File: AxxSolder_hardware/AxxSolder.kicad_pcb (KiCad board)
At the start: 2 copper layers, 39 x 82.5 mm, 138 parts, among them IC1 TLV76733DRVR, IC2 OPA2387DSGT, IC3 LMR54406DBVR, IC4 STM32G431CBT6, IC5 TPD4E1U06DBVR, IC6 STUSB4500QTR, IC7 MAX16171ATA_VY+T, IC8 LTC4440AHMS8E, IC9 INA180A4IDBVT, J1 USB4110-GF-A, J2 691243110009, J3 TSW-102-07-T-S, J4 61300611821, J5 TSW-102-07-T-S, J6 TSW-102-07-T-S, Q1 STL9P3LLH6, Q2 STL10N3LLH5, Q3 2N7002NXAKR, U2 PEC11J-9215F-S0015, U3 BSC014N04LS

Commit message: Change IC9 from INA180 to INA281
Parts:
- IC9: value INA180A4IDBVT -> INA281A5QDBVRQ1
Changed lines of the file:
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@@
       (net 27 "/CC2") (pinfunction "1") (pintype "passive"))
   )
-  (footprint "footprints:SOT95P280X145-5N" (layer "B.Cu")
-    (at 188.95 107)
-    (descr "DBV (R-PDSO-G5)")
-    (tags "Integrated Circuit")
-    (property "Height" "1.45")
-    (property "Manufacturer_Name" "Texas Instruments")
-    (property "Manufacturer_Part_Number" "INA180A4IDBVT")
-    (property "Mouser Part Number" "595-INA180A4IDBVT")
-    (property "Mouser Price/Stock" "https://www.mouser.co.uk/ProductDetail/Texas-Instruments/INA180A4IDBVT?qs=5aG0NVq1C4zRWLlwoLPFOA%3D%3D")
-    (property "Sheetfile" "AxxSolder.kicad_sch")
-    (property "Sheetname" "")
-    (property "ki_description" "26V, 350kHz Bandwidth, Low- or High-Side Voltage Output Current Sense Amplifier")
-    (attr smd)
-    (fp_text reference "IC9" (at -0.55 2.35) (layer "B.SilkS")
-        (effects (font (size 0.8 0.8) (thickness 0.15) bold) (justify mirror))
-    )
-    (fp_text value "INA180A4IDBVT" (at 0 0) (layer "B.SilkS") hide
-        (effects (font (size 1.27 1.27) (thickness 0.254)) (justify mirror))
-    )
-    (fp_text user "${REFERENCE}" (at 0 0) (layer "B.Fab")
-        (effects (font (size 1.27 1.27) (thickness 0.254)) (justify mirror))
-    )
-    (fp_line (start -1.85 1.5) (end -0.65 1.5)
-      (stroke (width 0.2) (type solid)) (layer "B.SilkS"))
-    (fp_line (start -0.3 -1.45) (end -0.3 1.45)
-      (stroke (width 0.2) (type solid)) (layer "B.SilkS"))
-    (fp_line (start -0.3 1.45) (end 0.3 1.45)
-      (stroke (width 0.2) (type solid)) (layer "B.SilkS"))
-    (fp_line (start 0.3 -1.45) (end -0.3 -1.45)
-      (stroke (width 0.2) (type solid)) (layer "B.SilkS"))
-    (fp_line (start 0.3 1.45) (end 0.3 -1.45)
-      (stroke (width 0.2) (type solid)) (layer "B.SilkS"))
-    (fp_line (start -2.1 -1.775) (end -2.1 1.775)
-      (stroke (width 0.05) (type solid)) (layer "B.CrtYd"))
-    (fp_line (start -2.1 1.775) (end 2.1 1.775)
-      (stroke (width 0.05) (type solid)) (layer "B.CrtYd"))
-    (fp_line (start 2.1 -1.775) (end -2.1 -1.775)
-      (stroke (width 0.05) (type solid)) (layer "B.CrtYd"))
-    (fp_line (start 2.1 1.775) (end 2.1 -1.775)
-      (stroke (width 0.05) (type solid)) (layer "B.CrtYd"))
-    (fp_line (start -0.8 -1.45) (end -0.8 1.45)
-      (stroke (width 0.1) (type solid)) (layer "B.Fab"))
-    (fp_line (start -0.8 0.5) (end 0.15 1.45)
-      (stroke (width 0.1) (type solid)) (layer "B.Fab"))
-    (fp_line (start -0.8 1.45) (end 0.8 1.45)
-      (stroke (width 0.1) (type solid)) (layer "B.Fab"))
-    (fp_line (start 0.8 -1.45) (end -0.8 -1.45)
-      (stroke (width 0.1) (type solid)) (layer "B.Fab"))
-    (fp_line (start 0.8 1.45) (end 0.8 -1.45)
-      (stroke (width 0.1) (type solid)) (layer "B.Fab"))
-    (pad "1" smd rect (at -1.25 0.95 270) (size 0.6 1.2) (layers "B.Cu" "B.Paste" "B.Mask")
-      (net 81 "/I_LEAK") (pinfunction "OUT") (pintype "output"))
-    (pad "2" smd rect (at -1.25 0 270) (size 0.6 1.2) (layers "B.Cu" "B.Paste" "B.Mask")
-      (net 15 "GND") (pinfunction "GND") (pintype "power_in"))
-    (pad "3" smd rect (at -1.25 -0.95 270) (size 0.6 1.2) (layers "B.Cu" "B.Paste" "B.Mask")
-      (net 82 "Net-(IC9-IN+)") (pinfunction "IN+") (pintype "input"))
-    (pad "4" smd rect (at 1.25 -0.95 270) (size 0.6 1.2) (layers "B.Cu" "B.Paste" "B.Mask")
-      (net 63 "Earth") (pinfunction "IN-") (pintype "input"))
-    (pad "5" smd rect (at 1.25 0.95 270) (size 0.6 1.2) (layers "B.Cu" "B.Paste" "B.Mask")
-      (net 2 "+3.3V") (pinfunction "VS") (pintype "power_in"))
-    (model "${KIPRJMOD}/3rd-parties-libraries/3D-models/INA180A4IDBVT.stp"
-      (offset (xyz 0 0 0))
-      (scale (xyz 1 1 1))
-      (rotate (xyz 0 0 0))
-    )
-  )
   (footprint "Resistor_SMD:R_0805_2012Metric" (layer "B.Cu")
     (at 189.6 103.1125 90)
@@
       (offset (xyz 0 0 0))
       (scale (xyz 1 1 1))
+      (rotate (xyz 0 0 0))
+    )
+  )
+  (footprint "footprints:SOT95P280X145-5N" (layer "B.Cu")
+    (at 188.95 107)
+    (descr "DBV (R-PDSO-G5)")
+    (tags "Integrated Circuit")
+    (property "Height" "1.45")
+    (property "Manufacturer_Name" "Texas Instruments")
+    (property "Manufacturer_Part_Number" "INA281A5QDBVRQ1")
+    (property "Mouser Part Number" "595-INA281A5QDBVRQ1")
+    (property "Mouser Price/Stock" "https://www.mouser.co.uk/ProductDetail/Texas-Instruments/INA281A5QDBVRQ1?qs=hd1VzrDQEGgwv71iGabWgQ%3D%3D")
+    (property "Sheetfile" "AxxSolder.kicad_sch")
+    (property "Sheetname" "")
+    (property "ki_description" "Current Sense Amplifiers Automotive AEC-Q100, -4-V to 110-V, 1.3-MHz current sense amplifier 5-SOT-23 -40 to 125")
+    (attr smd)
+    (fp_text reference "IC9" (at -0.87 2.29) (layer "B.SilkS")
+        (effects (font (size 0.8 0.8) (thickness 0.15) bold) (justify mirror))
+    )
+    (fp_text value "INA281A5QDBVRQ1" (at 0 0) (layer "B.SilkS") hide
+        (effects (font (size 1.27 1.27) (thickness 0.254)) (justify mirror))
+    )
+    (fp_text user "${REFERENCE}" (at 0 0) (layer "B.Fab")
+        (effects (font (size 1.27 1.27) (thickness 0.254)) (justify mirror))
+    )
+    (fp_line (start -1.85 1.5) (end -0.65 1.5)
+      (stroke (width 0.2) (type solid)) (layer "B.SilkS"))
+    (fp_line (start -0.3 -1.45) (end -0.3 1.45)
+      (stroke (width 0.2) (type solid)) (layer "B.SilkS"))
+    (fp_line (start -0.3 1.45) (end 0.3 1.45)
+      (stroke (width 0.2) (type solid)) (layer "B.SilkS"))
+    (fp_line (start 0.3 -1.45) (end -0.3 -1.45)
+      (stroke (width 0.2) (type solid)) (layer "B.SilkS"))
+    (fp_line (start 0.3 1.45) (end 0.3 -1.45)
+      (stroke (width 0.2) (type solid)) (layer "B.SilkS"))
+    (fp_line (start -2.1 -1.775) (end -2.1 1.775)
+      (stroke (width 0.05) (type solid)) (layer "B.CrtYd"))
+    (fp_line (start -2.1 1.775) (end 2.1 1.775)
+      (stroke (width 0.05) (type solid)) (layer "B.CrtYd"))
+    (fp_line (start 2.1 -1.775) (end -2.1 -1.775)
+      (stroke (width 0.05) (type solid)) (layer "B.CrtYd"))
+    (fp_line (start 2.1 1.775) (end 2.1 -1.775)
+      (stroke (width 0.05) (type solid)) (layer "B.CrtYd"))
+    (fp_line (start -0.8 -1.45) (end -0.8 1.45)
+      (stroke (width 0.1) (type solid)) (layer "B.Fab"))
+    (fp_line (start -0.8 0.5) (end 0.15 1.45)
+      (stroke (width 0.1) (type solid)) (layer "B.Fab"))
+    (fp_line (start -0.8 1.45) (end 0.8 1.45)
+      (stroke (width 0.1) (type solid)) (layer "B.Fab"))
+    (fp_line (start 0.8 -1.45) (end -0.8 -1.45)
+      (stroke (width 0.1) (type solid)) (layer "B.Fab"))
+    (fp_line (start 0.8 1.45) (end 0.8 -1.45)
+      (stroke (width 0.1) (type solid)) (layer "B.Fab"))
+    (pad "1" smd rect (at -1.25 0.95 270) (size 0.6 1.2) (layers "B.Cu" "B.Paste" "B.Mask")
+      (net 81 "/I_LEAK") (pinfunction "OUT") (pintype "passive"))
+    (pad "2" smd rect (at -1.25 0 270) (size 0.6 1.2) (layers "B.Cu" "B.Paste" "B.Mask")
+      (net 15 "GND") (pinfunction "GND") (pintype "passive"))
+    (pad "3" smd rect (at -1.25 -0.95 270) (size 0.6 1.2) (layers "B.Cu" "B.Paste" "B.Mask")
+      (net 82 "Net-(IC9-IN+)") (pinfunction "IN+") (pintype "passive"))
+    (pad "4" smd rect (at 1.25 -0.95 270) (size 0.6 1.2) (layers "B.Cu" "B.Paste" "B.Mask")
+      (net 63 "Earth") (pinfunction "IN-") (pintype "passive"))
+    (pad "5" smd rect (at 1.25 0.95 270) (size 0.6 1.2) (layers "B.Cu" "B.Paste" "B.Mask")
+      (net 2 "+3.3V") (pinfunction "VS") (pintype "passive"))
+    (model "${KIPRJMOD}/3rd-parties-libraries/3D-models/INA180A4IDBVT.stp"
+      (offset (xyz 0 0 0))
+      (scale (xyz 1 1 1))

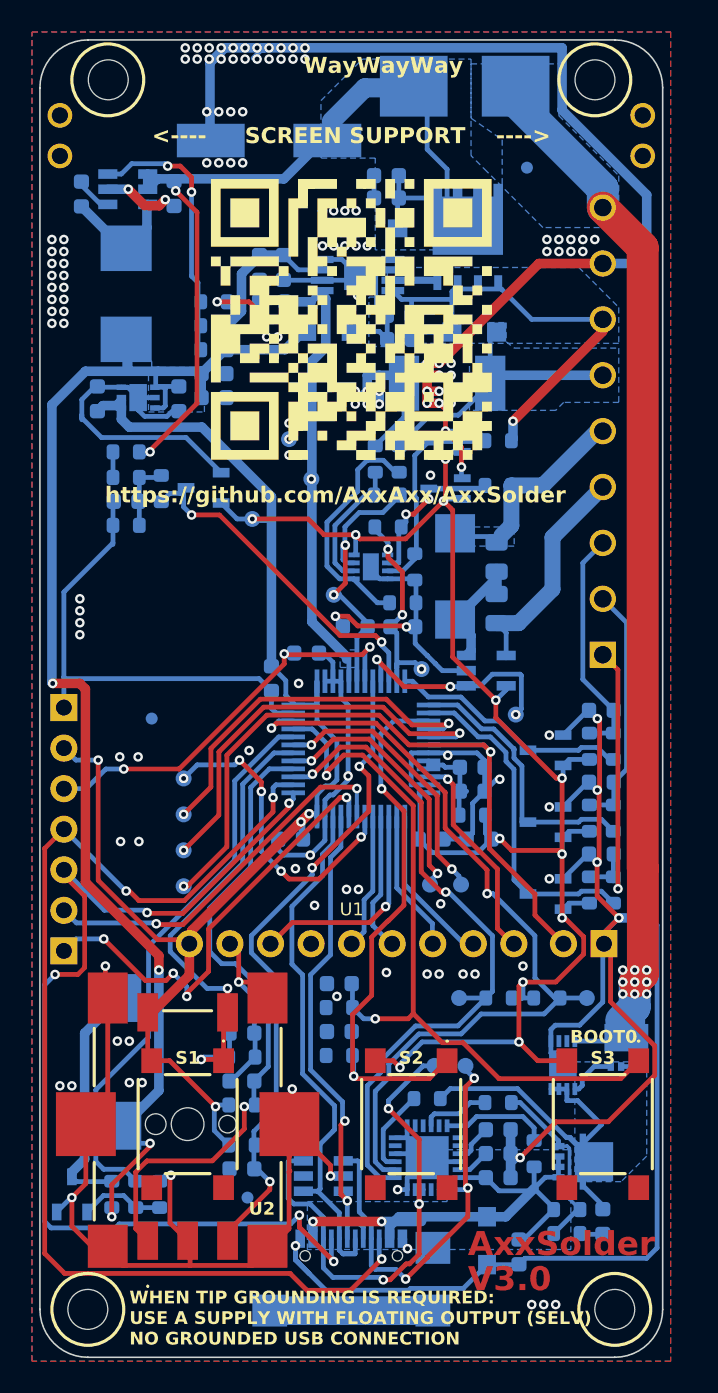
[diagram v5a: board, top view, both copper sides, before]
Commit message: Minor updates on PCB layout such as silkscreen placement and trace alignment
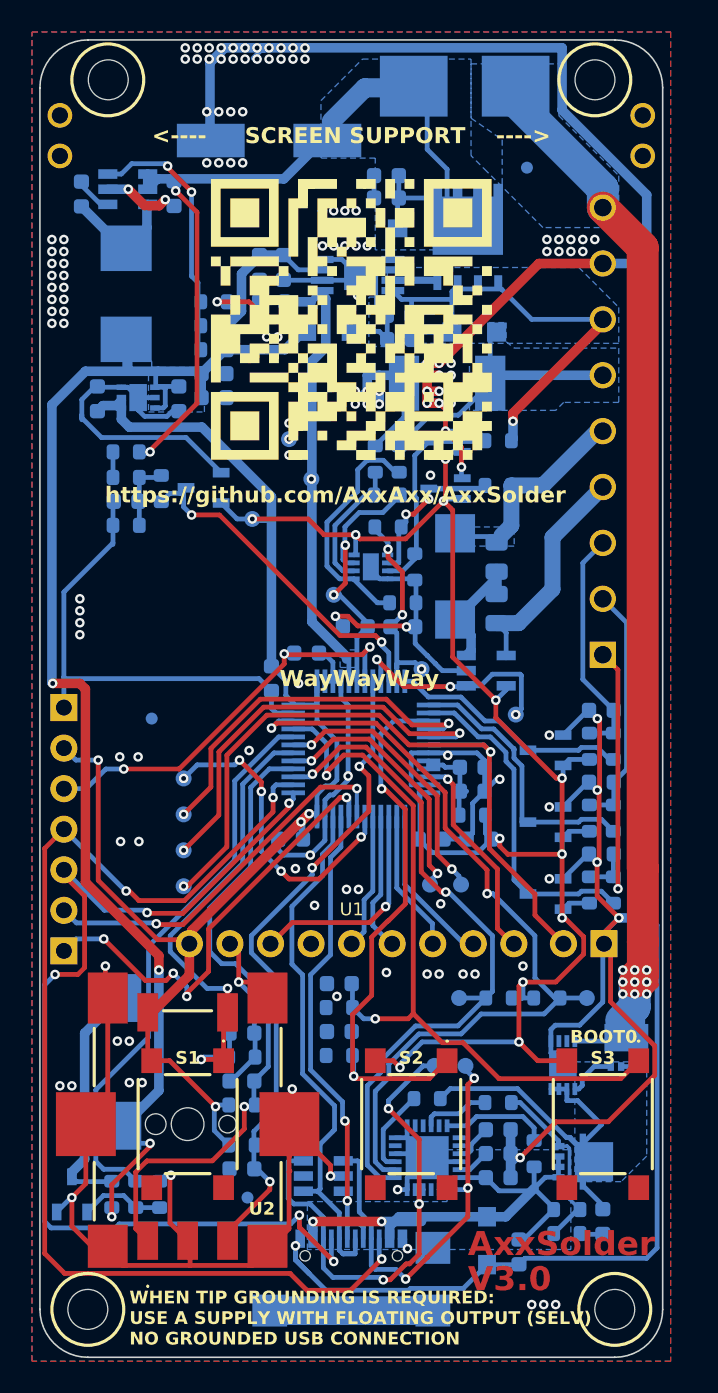
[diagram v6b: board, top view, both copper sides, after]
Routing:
- net /VDD_IN: track 65.8 -> 70.6 mm

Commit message: Update position of Display standoffs and minor PCB layout improvements
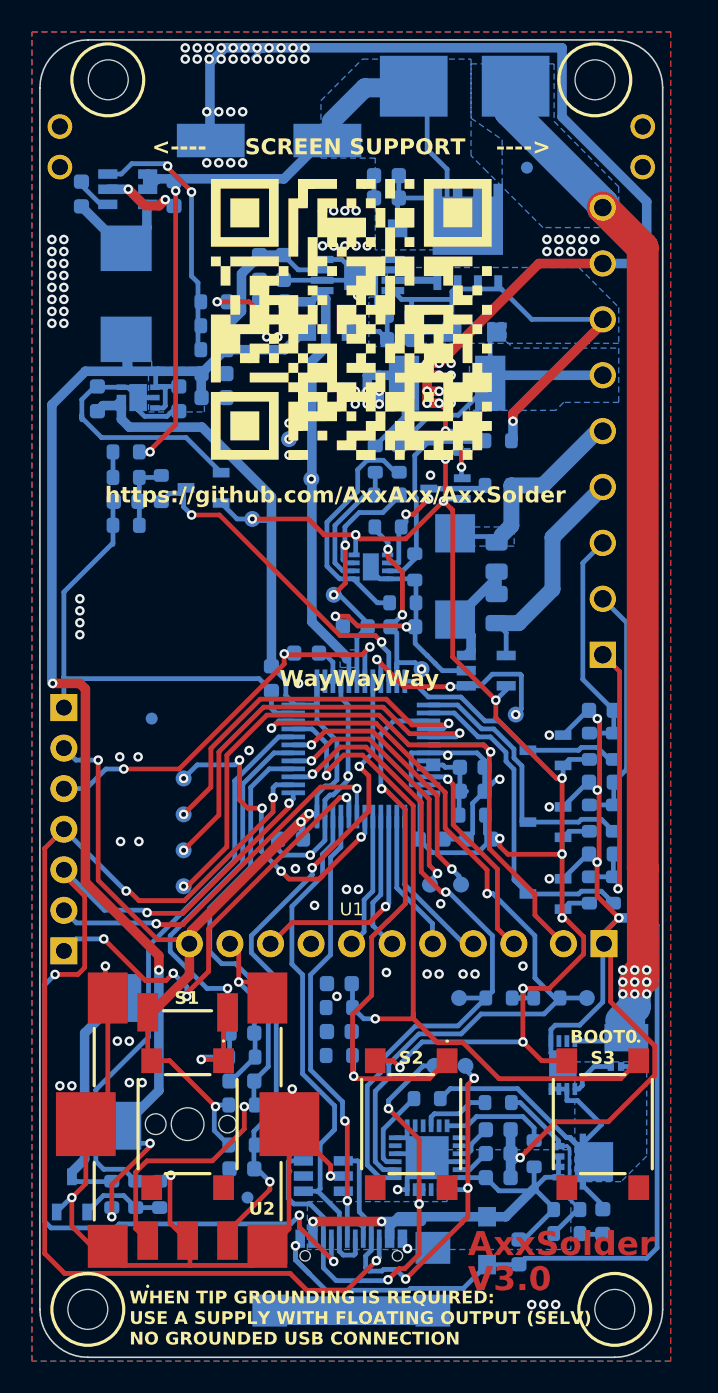
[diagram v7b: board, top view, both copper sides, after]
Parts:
- moved J5 0.70 mm to (162.2, 72.9)
- moved J6 0.70 mm to (198.8, 72.9)
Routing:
- net /VDD_IN: track 70.6 -> 71.9 mm
- net VDD: track 59.9 -> 58.8 mm
- net +3.3V: track 200.1 -> 199.4 mm
- net /CC1: track 27.5 -> 28.2 mm
- net /USB_D+: track 34.0 -> 33.4 mm
- net /USR1: track 19.7 -> 20.3 mm

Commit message: Add series resistance to button RC filters on schematic and board layout
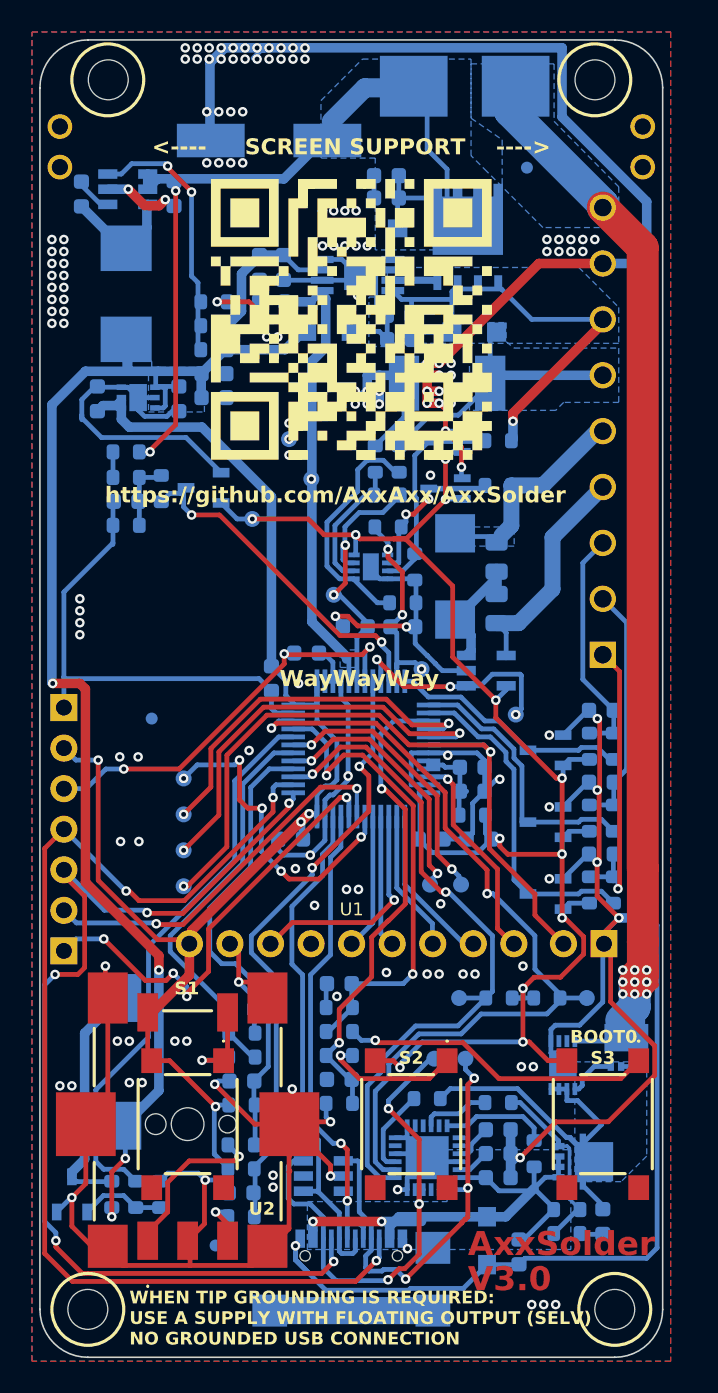
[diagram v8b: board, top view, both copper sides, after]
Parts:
- added R16: 100, Resistor_SMD:R_0603_1608Metric, B.Cu at (173.7, 131.2)
- added R43: 100, Resistor_SMD:R_0603_1608Metric, B.Cu at (179.8, 131.1)
- added R46: 100, Resistor_SMD:R_0603_1608Metric, B.Cu at (179.8, 129.6)
- added R47: 100, Resistor_SMD:R_0603_1608Metric, B.Cu at (173.6, 136.7)
- added R48: 100, Resistor_SMD:R_0603_1608Metric, B.Cu at (173.6, 141.2)
- moved FID2 3.61 mm to (172.0, 143.0)
- moved C22 3.00 mm to (179.8, 132.6)
- moved R31 3.00 mm to (179.8, 134.1)
- moved C29 1.50 mm to (173.6, 139.7)
- moved C21 1.50 mm to (173.7, 128.2)
- moved R30 1.50 mm to (173.7, 129.7)
- moved R36 1.49 mm to (173.6, 138.2)
- moved TP7 0.45 mm to (187.7, 131.3)
- moved TP8 0.45 mm to (185.7, 131.3)
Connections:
- J1 pad S1: unconnected-(J1-SHIELD-PadS1) -> (no net)
- S1 pad 1: /SW1 -> /S1
- S2 pad 1: /SW2 -> Net-(R43-Pad2)
- S3 pad 1: /SW3 -> Net-(R46-Pad2)
- U2 pad A1: /ENC_B -> Net-(R47-Pad2)
- U2 pad C1: /ENC_A -> Net-(R48-Pad2)
- U2 pad E1: /SW1 -> /S1
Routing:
- net Net-(R46-Pad2): track 0.00 -> 19.7 mm, vias 0 -> 1
- net /SW3: track 47.3 -> 30.4 mm
- net GND: track 447.9 -> 460.3 mm, vias 149 -> 157
- net /ENC_B: track 41.0 -> 29.0 mm, vias 1 -> 0
- net Net-(R47-Pad2): track 0.00 -> 10.3 mm, vias 0 -> 1
- net (no net): track 0.00 -> 10.2 mm
- net unconnected-(J1-SHIELD-PadS1): track 10.2 -> 0.00 mm
- net Net-(R43-Pad2): track 0.00 -> 9.08 mm, vias 0 -> 1
- net /SW2: track 36.6 -> 30.1 mm
- net /S1: track 0.00 -> 6.25 mm, vias 0 -> 1
- net /SW1: track 30.3 -> 25.3 mm, vias 2 -> 0
- net /ENC_A: track 41.5 -> 38.3 mm, vias 3 -> 2
- net Net-(R48-Pad2): track 0.00 -> 2.95 mm, vias 0 -> 1
- net +7.5V: track 95.8 -> 94.1 mm
- net /USB_D+: track 33.4 -> 32.5 mm
